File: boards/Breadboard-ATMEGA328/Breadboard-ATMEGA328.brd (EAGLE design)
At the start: 15.2 x 45.7 mm, 12 parts, among them IC1 ATMEGA328P-PU, J1 PINHD-1X7, J2 PINHD-1X7, J3 PINHD-1X7, J4 PINHD-1X7

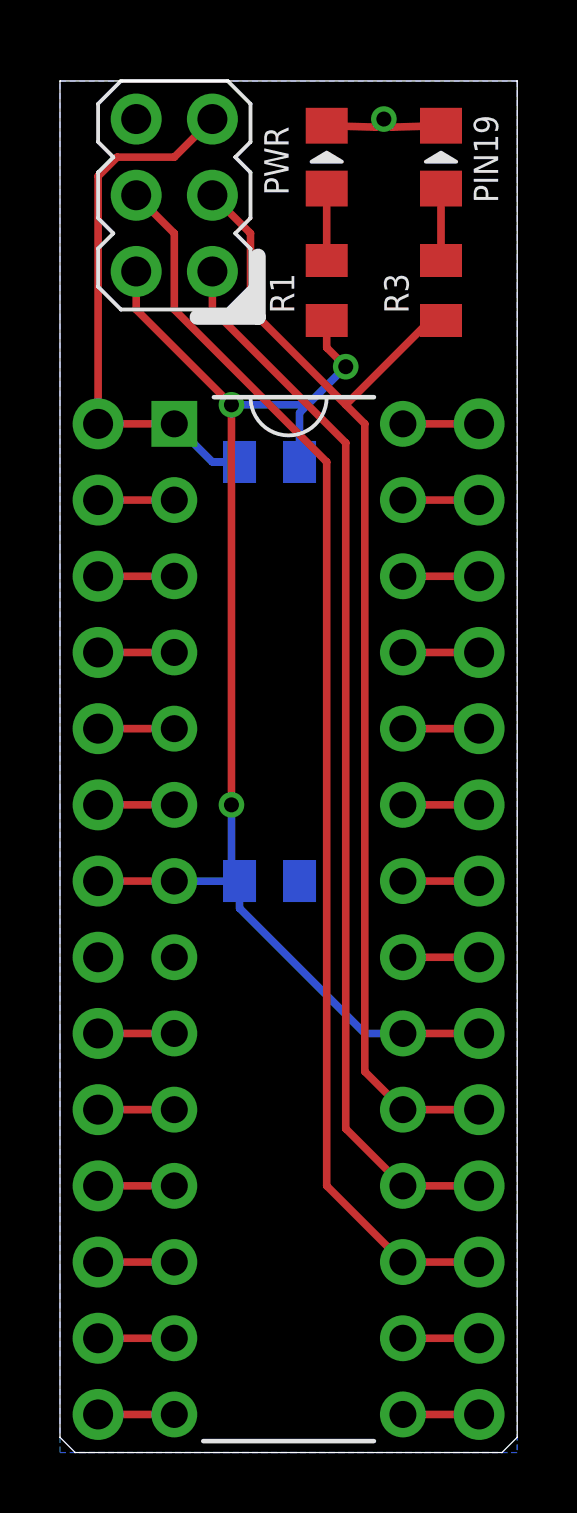
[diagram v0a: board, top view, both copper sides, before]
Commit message: Add a bit of space to breadboard adapters to ICSP connector will fit
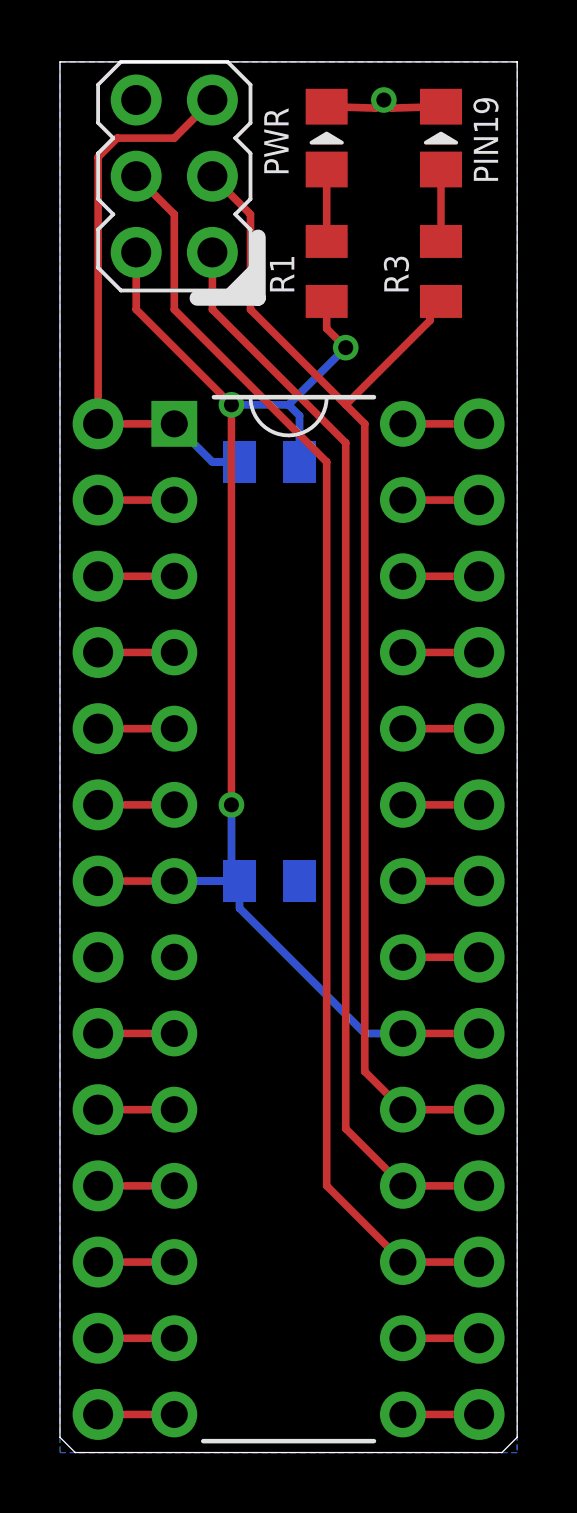
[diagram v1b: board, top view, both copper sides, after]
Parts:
- moved ISP1 0.64 mm to (3.81, 42.5)
- moved D1 0.63 mm to (8.89, 43.8)
- moved D2 0.63 mm to (12.7, 43.8)
- moved R1 0.63 mm to (8.89, 39.4)
- moved R3 0.63 mm to (12.7, 39.4)
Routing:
- net SCK: track 40.0 -> 41.3 mm
- net VCC: track 45.2 -> 46.2 mm
- net MOSI: track 41.8 -> 42.4 mm
- net MISO: track 35.7 -> 36.3 mm
- net RST: track 18.1 -> 18.7 mm
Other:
- board size 15.2 x 45.7 mm -> 15.2 x 46.4 mm
- board text added: "v1.2"
- board text removed: "v1.1"
